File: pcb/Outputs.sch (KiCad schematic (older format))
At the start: 58 parts, among them P66 IG2, P67 IG1, P81 IG3, P82 IG4, P84 Ignitor2, P85 Ignitor1, P86 Ignitor3, P87 Ignitor4, U10 VNS3NV04D, U12 TC442XA, U14 VNS3NV04D, U5 VN5E160AS-E, U9 TC442XA

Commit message: Finished placement and routing of low side drivers on PCB, ran DRC and found no errors.
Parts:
- removed D50, D51: LED, symbol LED
- removed R64, R65: 2.4k, symbol R
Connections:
- wire segments 78 -> 72
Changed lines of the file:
@@
 Sheet 5 7
 Title "Jaguar PCB for FreeEMS"
-Date "5 mar 2014"
+Date "6 mar 2014"
 Rev "0.7-alpha"
 Comp "Git: xxxxxxxxxx"
@@
 $EndComp
 $Comp
-L GND #PWR40
+L GND #PWR029
 U 1 1 509C8648
 P 7700 4100
-F 0 "#PWR40" H 7700 4100 30  0001 C CNN
+F 0 "#PWR029" H 7700 4100 30  0001 C CNN
 F 1 "GND" H 7700 4030 30  0001 C CNN
 F 2 "" H 7700 4100 60  0001 C CNN
@@
 $EndComp
 $Comp
-L GND #PWR36
+L GND #PWR030
 U 1 1 509C8647
 P 7550 2900
-F 0 "#PWR36" H 7550 2900 30  0001 C CNN
+F 0 "#PWR030" H 7550 2900 30  0001 C CNN
 F 1 "GND" H 7550 2830 30  0001 C CNN
 F 2 "" H 7550 2900 60  0001 C CNN
@@
 $EndComp
 $Comp
-L GND #PWR39
+L GND #PWR031
 U 1 1 509C8646
 P 7700 3450
-F 0 "#PWR39" H 7700 3450 30  0001 C CNN
+F 0 "#PWR031" H 7700 3450 30  0001 C CNN
 F 1 "GND" H 7700 3380 30  0001 C CNN
 F 2 "" H 7700 3450 60  0001 C CNN
@@
 $EndComp
 $Comp
-L GND #PWR44
+L GND #PWR032
 U 1 1 509C8641
 P 9800 3900
-F 0 "#PWR44" H 9800 3900 30  0001 C CNN
+F 0 "#PWR032" H 9800 3900 30  0001 C CNN
 F 1 "GND" H 9800 3830 30  0001 C CNN
 F 2 "" H 9800 3900 60  0001 C CNN
@@
 JP1 selects either\n5v or 12v \nDriver IC Supply
 $Comp
-L GND #PWR43
+L GND #PWR033
 U 1 1 5092C12A
 P 9800 1950
-F 0 "#PWR43" H 9800 1950 30  0001 C CNN
+F 0 "#PWR033" H 9800 1950 30  0001 C CNN
 F 1 "GND" H 9800 1880 30  0001 C CNN
 F 2 "" H 9800 1950 60  0001 C CNN
@@
 $EndComp
 $Comp
-L GND #PWR37
+L GND #PWR034
 U 1 1 5092BF20
 P 7700 1500
-F 0 "#PWR37" H 7700 1500 30  0001 C CNN
+F 0 "#PWR034" H 7700 1500 30  0001 C CNN
 F 1 "GND" H 7700 1430 30  0001 C CNN
 F 2 "" H 7700 1500 60  0001 C CNN
@@
 $EndComp
 $Comp
-L GND #PWR35
+L GND #PWR035
 U 1 1 5092BF13
 P 7550 950
-F 0 "#PWR35" H 7550 950 30  0001 C CNN
+F 0 "#PWR035" H 7550 950 30  0001 C CNN
 F 1 "GND" H 7550 880 30  0001 C CNN
 F 2 "" H 7550 950 60  0001 C CNN
@@
 $EndComp
 $Comp
-L GND #PWR38
+L GND #PWR036
 U 1 1 5092BF09
 P 7700 2150
-F 0 "#PWR38" H 7700 2150 30  0001 C CNN
+F 0 "#PWR036" H 7700 2150 30  0001 C CNN
 F 1 "GND" H 7700 2080 30  0001 C CNN
 F 2 "" H 7700 2150 60  0001 C CNN
@@
 12vdc-switched-outputs
 $Comp
-L GND #PWR30
+L GND #PWR037
 U 1 1 4F2F3E3F
 P 1100 5500
-F 0 "#PWR30" H 1100 5500 30  0001 C CNN
+F 0 "#PWR037" H 1100 5500 30  0001 C CNN
 F 1 "GND" H 1100 5430 30  0001 C CNN
 F 2 "" H 1100 5500 60  0001 C CNN
@@
 $EndComp
 $Comp
-L GND #PWR29
+L GND #PWR038
 U 1 1 4F2F3E2D
 P 1100 3650
-F 0 "#PWR29" H 1100 3650 30  0001 C CNN
+F 0 "#PWR038" H 1100 3650 30  0001 C CNN
 F 1 "GND" H 1100 3580 30  0001 C CNN
 F 2 "" H 1100 3650 60  0001 C CNN
@@
 $EndComp
 $Comp
-L GND #PWR31
+L GND #PWR039
 U 1 1 4F2F3E0C
 P 1200 1850
-F 0 "#PWR31" H 1200 1850 30  0001 C CNN
+F 0 "#PWR039" H 1200 1850 30  0001 C CNN
 F 1 "GND" H 1200 1780 30  0001 C CNN
 F 2 "" H 1200 1850 60  0001 C CNN
@@
 	1    0    0    -1
 $EndComp
-Connection ~ 9050 900
-$Comp
-L LED D50
-U 1 1 52F2735A
-P 8850 900
-F 0 "D50" H 8850 1000 40  0000 C CNN
-F 1 "LED" H 8850 800 40  0000 C CNN
-F 2 "" H 8850 900 60  0001 C CNN
-F 3 "" H 8850 900 60  0001 C CNN
-	1    8850 900
-	-1   0    0    1
-$EndComp
-$Comp
-L R R64
-U 1 1 52F27360
-P 9300 900
-F 0 "R64" V 9380 900 40  0000 C CNN
-F 1 "2.4k" V 9300 900 40  0000 C CNN
-F 2 "" H 9300 900 60  0001 C CNN
-F 3 "" H 9300 900 60  0001 C CNN
-	1    9300 900
-	0    -1   -1   0
-$EndComp
-Connection ~ 9050 2100
-$Comp
-L LED D51
-U 1 1 52F27367
-P 8850 2100
-F 0 "D51" H 8850 2200 40  0000 C CNN
-F 1 "LED" H 8850 2000 40  0000 C CNN
-F 2 "" H 8850 2100 60  0001 C CNN
-F 3 "" H 8850 2100 60  0001 C CNN
-	1    8850 2100
-	-1   0    0    1
-$EndComp
-$Comp
-L R R65
-U 1 1 52F2736D
-P 9300 2100
-F 0 "R65" V 9380 2100 40  0000 C CNN
-F 1 "2.4k" V 9300 2100 40  0000 C CNN
-F 2 "" H 9300 2100 60  0001 C CNN
-F 3 "" H 9300 2100 60  0001 C CNN
-	1    9300 2100
-	0    -1   -1   0
-$EndComp
-Wire Wire Line
-	9550 900  9550 1400
-Wire Wire Line
-	9550 1400 9500 1400
-Wire Wire Line
-	9550 2100 9550 1600
-Wire Wire Line
-	9550 1600 9500 1600
-$Comp
-L GND #PWR41
-U 1 1 52F274AB
-P 8650 950
-F 0 "#PWR41" H 8650 950 30  0001 C CNN
-F 1 "GND" H 8650 880 30  0001 C CNN
-F 2 "" H 8650 950 60  0001 C CNN
-F 3 "" H 8650 950 60  0001 C CNN
-	1    8650 950
-	1    0    0    -1
-$EndComp
-$Comp
-L GND #PWR42
-U 1 1 52F274B1
-P 8650 2150
-F 0 "#PWR42" H 8650 2150 30  0001 C CNN
-F 1 "GND" H 8650 2080 30  0001 C CNN
-F 2 "" H 8650 2150 60  0001 C CNN
-F 3 "" H 8650 2150 60  0001 C CNN
-	1    8650 2150
-	1    0    0    -1
-$EndComp
-Wire Wire Line
-	8650 2150 8650 2100
-Wire Wire Line
-	8650 950  8650 900
-Connection ~ 9550 900
-Connection ~ 8650 900
-Connection ~ 8650 2100
-Connection ~ 9550 2100
 Wire Wire Line
 	9800 1900 9800 1950
@@
 Connection ~ 1650 3350
 $Comp
-L GND #PWR32
+L GND #PWR040
 U 1 1 52F28353
 P 1650 3850
-F 0 "#PWR32" H 1650 3850 30  0001 C CNN
+F 0 "#PWR040" H 1650 3850 30  0001 C CNN
 F 1 "GND" H 1650 3780 30  0001 C CNN
 F 2 "" H 1650 3850 60  0001 C CNN
@@
 PCB-GND
 $Comp
-L GND #PWR34
+L GND #PWR041
 U 1 1 52F2881A
 P 3200 900
-F 0 "#PWR34" H 3200 900 30  0001 C CNN
+F 0 "#PWR041" H 3200 900 30  0001 C CNN
 F 1 "GND" H 3200 830 30  0001 C CNN
 F 2 "" H 3200 900 60  0001 C CNN
@@
 Connection ~ 1650 5200
 $Comp
-L GND #PWR33
+L GND #PWR042
 U 1 1 52F26A48
 P 1650 5700
-F 0 "#PWR33" H 1650 5700 30  0001 C CNN
+F 0 "#PWR042" H 1650 5700 30  0001 C CNN
 F 1 "GND" H 1650 5630 30  0001 C CNN
 F 2 "" H 1650 5700 60  0001 C CNN

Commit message: Added ignitor outputs SMD resistors and LEDs for indicators, http://issues.freeems.org/view.php?id=888
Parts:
- added D50, D51, D52, D53: LED, symbol LED
- added R64, R65, R79, R85: 2.4k, symbol R
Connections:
- wire segments 72 -> 80
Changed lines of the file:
@@
 Sheet 5 7
 Title "Jaguar PCB for FreeEMS"
-Date "6 mar 2014"
+Date "7 mar 2014"
 Rev "0.7-alpha"
 Comp "Git: xxxxxxxxxx"
@@
 $EndComp
 $Comp
-L GND #PWR029
+L GND #PWR40
 U 1 1 509C8648
 P 7700 4100
-F 0 "#PWR029" H 7700 4100 30  0001 C CNN
+F 0 "#PWR40" H 7700 4100 30  0001 C CNN
 F 1 "GND" H 7700 4030 30  0001 C CNN
 F 2 "" H 7700 4100 60  0001 C CNN
@@
 $EndComp
 $Comp
-L GND #PWR030
+L GND #PWR36
 U 1 1 509C8647
 P 7550 2900
-F 0 "#PWR030" H 7550 2900 30  0001 C CNN
+F 0 "#PWR36" H 7550 2900 30  0001 C CNN
 F 1 "GND" H 7550 2830 30  0001 C CNN
 F 2 "" H 7550 2900 60  0001 C CNN
@@
 $EndComp
 $Comp
-L GND #PWR031
+L GND #PWR39
 U 1 1 509C8646
 P 7700 3450
-F 0 "#PWR031" H 7700 3450 30  0001 C CNN
+F 0 "#PWR39" H 7700 3450 30  0001 C CNN
 F 1 "GND" H 7700 3380 30  0001 C CNN
 F 2 "" H 7700 3450 60  0001 C CNN
@@
 $EndComp
 $Comp
-L GND #PWR032
+L GND #PWR42
 U 1 1 509C8641
 P 9800 3900
-F 0 "#PWR032" H 9800 3900 30  0001 C CNN
+F 0 "#PWR42" H 9800 3900 30  0001 C CNN
 F 1 "GND" H 9800 3830 30  0001 C CNN
 F 2 "" H 9800 3900 60  0001 C CNN
@@
 JP1 selects either\n5v or 12v \nDriver IC Supply
 $Comp
-L GND #PWR033
+L GND #PWR41
 U 1 1 5092C12A
 P 9800 1950
-F 0 "#PWR033" H 9800 1950 30  0001 C CNN
+F 0 "#PWR41" H 9800 1950 30  0001 C CNN
 F 1 "GND" H 9800 1880 30  0001 C CNN
 F 2 "" H 9800 1950 60  0001 C CNN
@@
 $EndComp
 $Comp
-L GND #PWR034
+L GND #PWR37
 U 1 1 5092BF20
 P 7700 1500
-F 0 "#PWR034" H 7700 1500 30  0001 C CNN
+F 0 "#PWR37" H 7700 1500 30  0001 C CNN
 F 1 "GND" H 7700 1430 30  0001 C CNN
 F 2 "" H 7700 1500 60  0001 C CNN
@@
 $EndComp
 $Comp
-L GND #PWR035
+L GND #PWR35
 U 1 1 5092BF13
 P 7550 950
-F 0 "#PWR035" H 7550 950 30  0001 C CNN
+F 0 "#PWR35" H 7550 950 30  0001 C CNN
 F 1 "GND" H 7550 880 30  0001 C CNN
 F 2 "" H 7550 950 60  0001 C CNN
@@
 $EndComp
 $Comp
-L GND #PWR036
+L GND #PWR38
 U 1 1 5092BF09
 P 7700 2150
-F 0 "#PWR036" H 7700 2150 30  0001 C CNN
+F 0 "#PWR38" H 7700 2150 30  0001 C CNN
 F 1 "GND" H 7700 2080 30  0001 C CNN
 F 2 "" H 7700 2150 60  0001 C CNN
@@
 12vdc-switched-outputs
 $Comp
-L GND #PWR037
+L GND #PWR30
 U 1 1 4F2F3E3F
 P 1100 5500
-F 0 "#PWR037" H 1100 5500 30  0001 C CNN
+F 0 "#PWR30" H 1100 5500 30  0001 C CNN
 F 1 "GND" H 1100 5430 30  0001 C CNN
 F 2 "" H 1100 5500 60  0001 C CNN
@@
 $EndComp
 $Comp
-L GND #PWR038
+L GND #PWR29
 U 1 1 4F2F3E2D
 P 1100 3650
-F 0 "#PWR038" H 1100 3650 30  0001 C CNN
+F 0 "#PWR29" H 1100 3650 30  0001 C CNN
 F 1 "GND" H 1100 3580 30  0001 C CNN
 F 2 "" H 1100 3650 60  0001 C CNN
@@
 $EndComp
 $Comp
-L GND #PWR039
+L GND #PWR31
 U 1 1 4F2F3E0C
 P 1200 1850
-F 0 "#PWR039" H 1200 1850 30  0001 C CNN
+F 0 "#PWR31" H 1200 1850 30  0001 C CNN
 F 1 "GND" H 1200 1780 30  0001 C CNN
 F 2 "" H 1200 1850 60  0001 C CNN
@@
 Connection ~ 1650 3350
 $Comp
-L GND #PWR040
+L GND #PWR32
 U 1 1 52F28353
 P 1650 3850
-F 0 "#PWR040" H 1650 3850 30  0001 C CNN
+F 0 "#PWR32" H 1650 3850 30  0001 C CNN
 F 1 "GND" H 1650 3780 30  0001 C CNN
 F 2 "" H 1650 3850 60  0001 C CNN
@@
 PCB-GND
 $Comp
-L GND #PWR041
+L GND #PWR34
 U 1 1 52F2881A
 P 3200 900
-F 0 "#PWR041" H 3200 900 30  0001 C CNN
+F 0 "#PWR34" H 3200 900 30  0001 C CNN
 F 1 "GND" H 3200 830 30  0001 C CNN
 F 2 "" H 3200 900 60  0001 C CNN
@@
 Connection ~ 1650 5200
 $Comp
-L GND #PWR042
+L GND #PWR33
 U 1 1 52F26A48
 P 1650 5700
-F 0 "#PWR042" H 1650 5700 30  0001 C CNN
+F 0 "#PWR33" H 1650 5700 30  0001 C CNN
 F 1 "GND" H 1650 5630 30  0001 C CNN
 F 2 "" H 1650 5700 60  0001 C CNN
@@
 Wire Notes Line
 	650  5950 650  4250
+Connection ~ 9200 850
+Connection ~ 8700 850
+Connection ~ 9600 850
+Text HLabel 8700 850  0    40   Input ~ 0
+12vdc-switched-outputs
+$Comp
+L R R64
+U 1 1 531922A3
+P 8950 850
+F 0 "R64" V 9030 850 40  0000 C CNN
+F 1 "2.4k" V 8950 850 40  0000 C CNN
+F 2 "" H 8950 850 60  0001 C CNN
+F 3 "" H 8950 850 60  0001 C CNN
+	1    8950 850
+	0    1    1    0
+$EndComp
+$Comp
+L LED D50
+U 1 1 531922A9
+P 9400 850
+F 0 "D50" H 9400 950 40  0000 C CNN
+F 1 "LED" H 9400 750 40  0000 C CNN
+F 2 "" H 9400 850 60  0001 C CNN
+F 3 "" H 9400 850 60  0001 C CNN
+	1    9400 850
+	1    0    0    -1
+$EndComp
+Connection ~ 9200 2150
+Connection ~ 8700 2150
+Connection ~ 9600 2150
+Text HLabel 8700 2150 0    40   Input ~ 0
+12vdc-switched-outputs
+$Comp
+L R R65
+U 1 1 531922BA
+P 8950 2150
+F 0 "R65" V 9030 2150 40  0000 C CNN
+F 1 "2.4k" V 8950 2150 40  0000 C CNN
+F 2 "" H 8950 2150 60  0001 C CNN
+F 3 "" H 8950 2150 60  0001 C CNN
+	1    8950 2150
+	0    1    1    0
+$EndComp
+$Comp
+L LED D51
+U 1 1 531922C0
+P 9400 2150
+F 0 "D51" H 9400 2250 40  0000 C CNN
+F 1 "LED" H 9400 2050 40  0000 C CNN
+F 2 "" H 9400 2150 60  0001 C CNN
+F 3 "" H 9400 2150 60  0001 C CNN
+	1    9400 2150
+	1    0    0    -1
+$EndComp
+Wire Wire Line
+	9600 850  9600 1400
+Wire Wire Line
+	9600 1400 9500 1400
+Wire Wire Line
+	9600 2150 9600 1600
+Wire Wire Line
+	9600 1600 9500 1600
+Connection ~ 9200 2800
+Connection ~ 8700 2800
+Connection ~ 9600 2800
+Text HLabel 8700 2800 0    40   Input ~ 0
+12vdc-switched-outputs
+$Comp
+L R R79
+U 1 1 531926CD
+P 8950 2800
+F 0 "R79" V 9030 2800 40  0000 C CNN
+F 1 "2.4k" V 8950 2800 40  0000 C CNN
+F 2 "" H 8950 2800 60  0001 C CNN
+F 3 "" H 8950 2800 60  0001 C CNN
+	1    8950 2800
+	0    1    1    0
+$EndComp
+$Comp
+L LED D52
+U 1 1 531926D3
+P 9400 2800
+F 0 "D52" H 9400 2900 40  0000 C CNN
+F 1 "LED" H 9400 2700 40  0000 C CNN
+F 2 "" H 9400 2800 60  0001 C CNN
+F 3 "" H 9400 2800 60  0001 C CNN
+	1    9400 2800
+	1    0    0    -1
+$EndComp
+Wire Wire Line
+	9600 2800 9600 3350
+Connection ~ 9200 4100
+Connection ~ 8700 4100
+Connection ~ 9600 4100
+Text HLabel 8700 4100 0    40   Input ~ 0
+12vdc-switched-outputs
+$Comp
+L R R85
+U 1 1 531926DE
+P 8950 4100
+F 0 "R85" V 9030 4100 40  0000 C CNN
+F 1 "2.4k" V 8950 4100 40  0000 C CNN
+F 2 "" H 8950 4100 60  0001 C CNN
+F 3 "" H 8950 4100 60  0001 C CNN
+	1    8950 4100
+	0    1    1    0
+$EndComp
+$Comp
+L LED D53
+U 1 1 531926E4
+P 9400 4100
+F 0 "D53" H 9400 4200 40  0000 C CNN
+F 1 "LED" H 9400 4000 40  0000 C CNN
+F 2 "" H 9400 4100 60  0001 C CNN
+F 3 "" H 9400 4100 60  0001 C CNN
+	1    9400 4100
+	1    0    0    -1
+$EndComp
+Wire Wire Line
+	9600 4100 9600 3550
+Wire Wire Line
+	9600 3550 9500 3550
+Wire Wire Line
+	9600 3350 9500 3350
 $EndSCHEMATC

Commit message: Corrected LED setup on ignitor outputs to go to ground, added diode to HSD output LED circuit, changed label called FAN to LSD2, added jumper to select using PK4 to LSD2 input, added jumper to select CPU Fuel Pump output port A7 to go to HSD or LSD4.
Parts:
- added D54: 1N4148, symbol DIODE
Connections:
- net labels added: LSD4, LSD4-IN
- net labels removed: Fan-IN, Fan_Relay
- wire segments 80 -> 88
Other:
- note added: "High Side Driver Relay Output"
- note added: "Low Side Driver #1 and #2 Outputs"
- note added: "Low Side Driver #3 and #4 Outputs"
- note removed: "Fuel Pump Relay Output"
- note removed: "Low Side Driver #2 and #3 Outputs"
- note removed: "Radiator Fan and Low Side Driver #1 Outputs"
- moved on the sheet: D30, D50, D51, D52, D53, R53, R64, R65, R79, R85

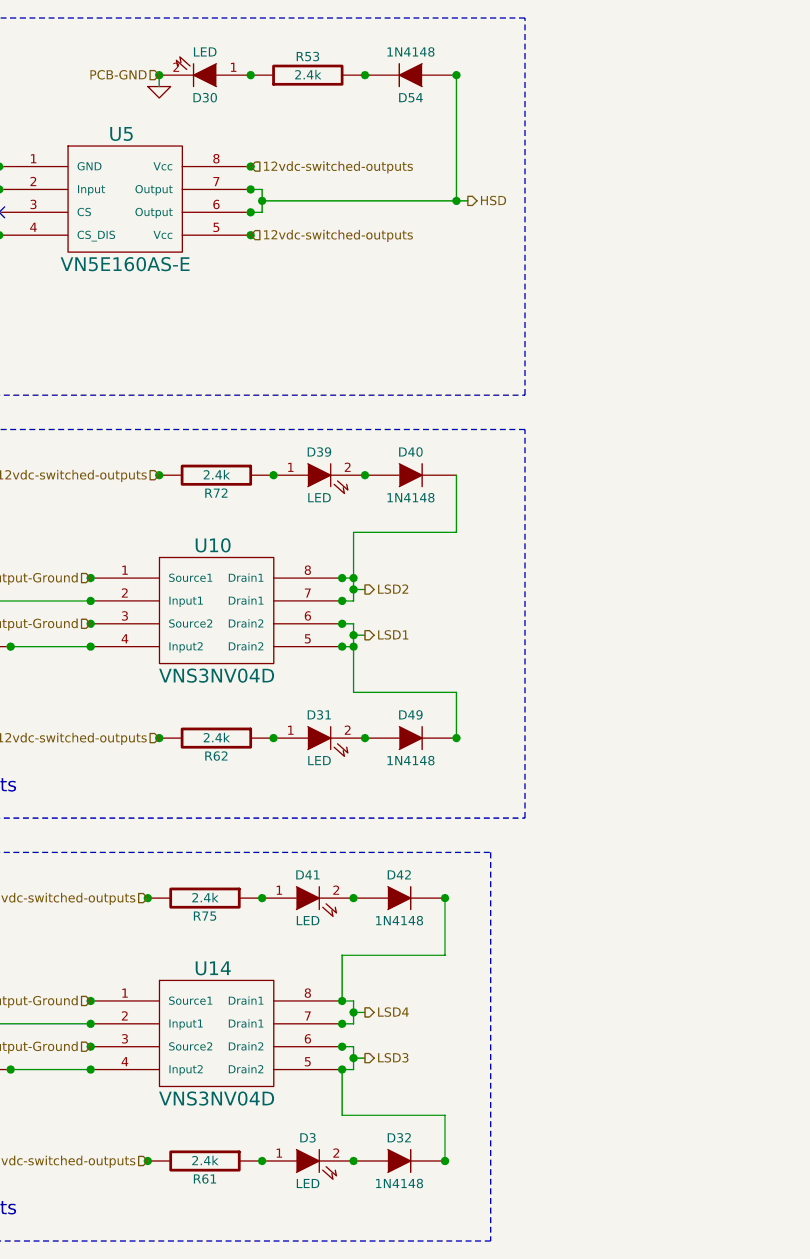
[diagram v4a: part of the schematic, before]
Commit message: Changed output LED protection diodes from 1N4148 package to 1N4001 (or other 1N400x) package.
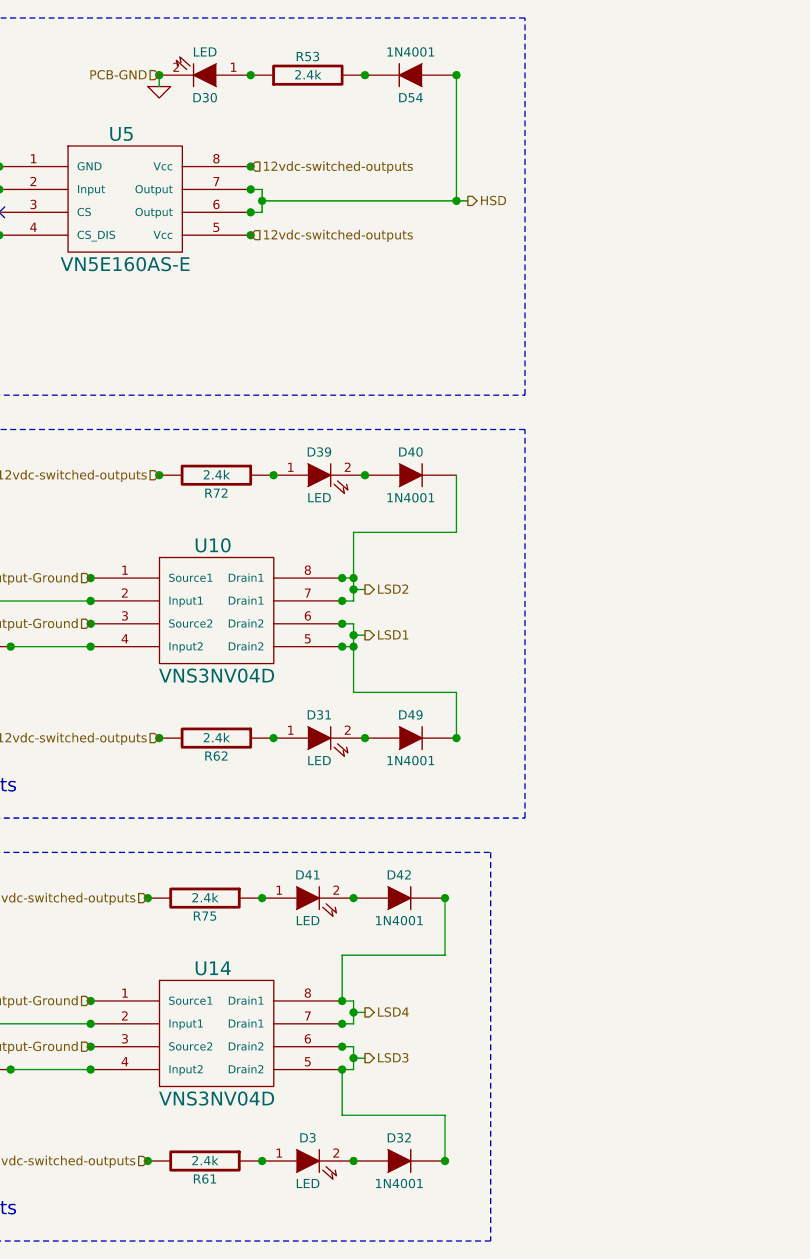
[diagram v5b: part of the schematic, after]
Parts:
- D32, D40, D42, D49, D54: value 1N4148 -> 1N4001
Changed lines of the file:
@@
 P 3850 4450
 F 0 "D42" H 3850 4550 40  0000 C CNN
-F 1 "1N4148" H 3850 4350 40  0000 C CNN
+F 1 "1N4001" H 3850 4350 40  0000 C CNN
 F 2 "" H 3850 4450 60  0001 C CNN
 F 3 "" H 3850 4450 60  0001 C CNN
@@
 P 3900 3750
 F 0 "D49" H 3900 3850 40  0000 C CNN
-F 1 "1N4148" H 3900 3650 40  0000 C CNN
+F 1 "1N4001" H 3900 3650 40  0000 C CNN
 F 2 "" H 3900 3750 60  0001 C CNN
 F 3 "" H 3900 3750 60  0001 C CNN
@@
 P 3900 2600
 F 0 "D40" H 3900 2700 40  0000 C CNN
-F 1 "1N4148" H 3900 2500 40  0000 C CNN
+F 1 "1N4001" H 3900 2500 40  0000 C CNN
 F 2 "" H 3900 2600 60  0001 C CNN
 F 3 "" H 3900 2600 60  0001 C CNN
@@
 P 3850 5600
 F 0 "D32" H 3850 5700 40  0000 C CNN
-F 1 "1N4148" H 3850 5500 40  0000 C CNN
+F 1 "1N4001" H 3850 5500 40  0000 C CNN
 F 2 "" H 3850 5600 60  0001 C CNN
 F 3 "" H 3850 5600 60  0001 C CNN
@@
 P 3900 850
 F 0 "D54" H 3900 950 40  0000 C CNN
-F 1 "1N4148" H 3900 750 40  0000 C CNN
+F 1 "1N4001" H 3900 750 40  0000 C CNN
 F 2 "" H 3900 850 60  0001 C CNN
 F 3 "" H 3900 850 60  0001 C CNN

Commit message: Updated schematics to show LED protection diodes as 1N4004 instead of 1N4001.
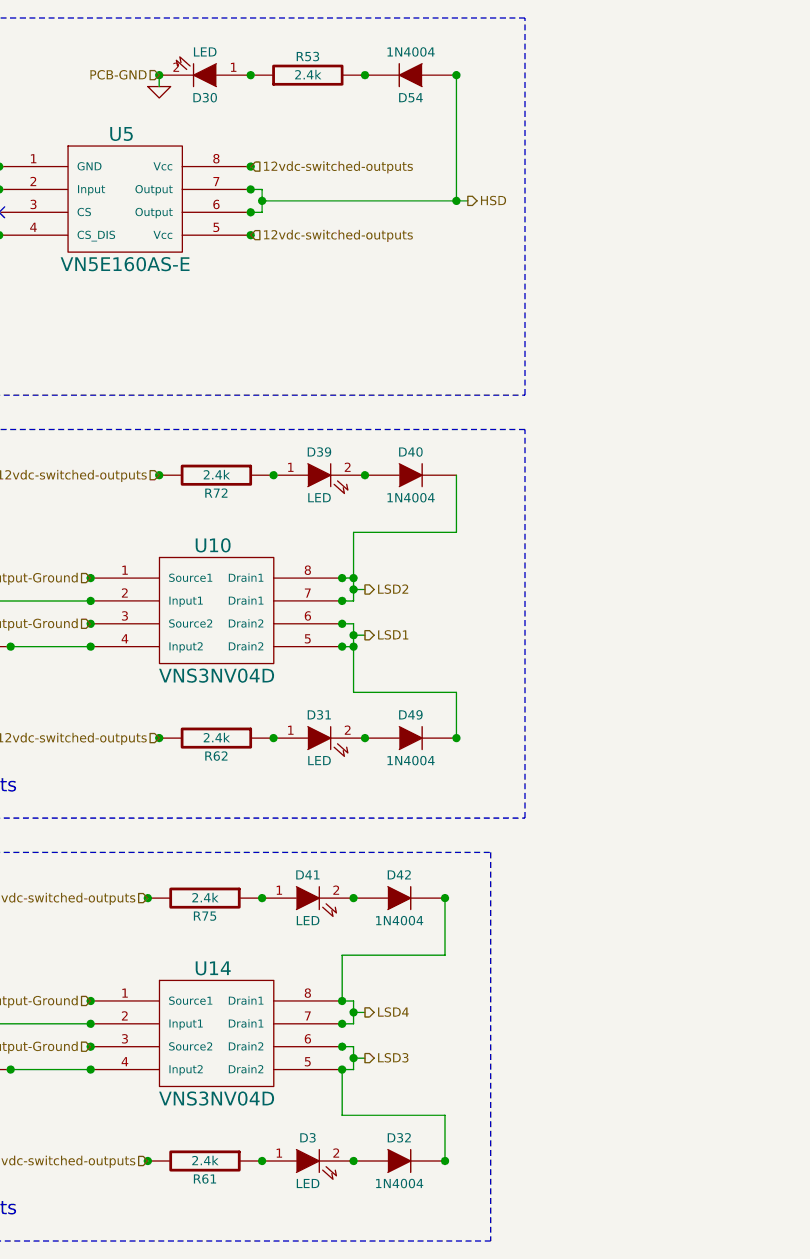
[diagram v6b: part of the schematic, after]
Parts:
- D32, D40, D42, D49, D54: value 1N4001 -> 1N4004
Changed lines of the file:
@@
 P 3850 4450
 F 0 "D42" H 3850 4550 40  0000 C CNN
-F 1 "1N4001" H 3850 4350 40  0000 C CNN
+F 1 "1N4004" H 3850 4350 40  0000 C CNN
 F 2 "" H 3850 4450 60  0001 C CNN
 F 3 "" H 3850 4450 60  0001 C CNN
@@
 P 3900 3750
 F 0 "D49" H 3900 3850 40  0000 C CNN
-F 1 "1N4001" H 3900 3650 40  0000 C CNN
+F 1 "1N4004" H 3900 3650 40  0000 C CNN
 F 2 "" H 3900 3750 60  0001 C CNN
 F 3 "" H 3900 3750 60  0001 C CNN
@@
 P 3900 2600
 F 0 "D40" H 3900 2700 40  0000 C CNN
-F 1 "1N4001" H 3900 2500 40  0000 C CNN
+F 1 "1N4004" H 3900 2500 40  0000 C CNN
 F 2 "" H 3900 2600 60  0001 C CNN
 F 3 "" H 3900 2600 60  0001 C CNN
@@
 P 3850 5600
 F 0 "D32" H 3850 5700 40  0000 C CNN
-F 1 "1N4001" H 3850 5500 40  0000 C CNN
+F 1 "1N4004" H 3850 5500 40  0000 C CNN
 F 2 "" H 3850 5600 60  0001 C CNN
 F 3 "" H 3850 5600 60  0001 C CNN
@@
 P 3900 850
 F 0 "D54" H 3900 950 40  0000 C CNN
-F 1 "1N4001" H 3900 750 40  0000 C CNN
+F 1 "1N4004" H 3900 750 40  0000 C CNN
 F 2 "" H 3900 850 60  0001 C CNN
 F 3 "" H 3900 850 60  0001 C CNN
